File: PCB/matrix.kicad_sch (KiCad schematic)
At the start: 103 parts, among them SW10 1u, SW100 1u, SW101 1u, SW102 1u, SW103 2u, SW104 1u, SW11 1u, SW12 1u, SW13 1u, SW14 1u, SW15 1u, SW16 1u, SW17 1u, SW18 1u, SW19 1u, SW2 1u, SW20 1u, SW21 1u, SW22 1u, SW23 1u, SW24 1u, SW25 1u, SW26 1u, SW27 1u, SW28 1u, SW29 1u, SW3 1u, SW30 1u, SW31 1u, SW32 1u, SW33 1.5u, SW34 1u, SW35 1u, SW36 1u, SW37 1u, SW38 1u, SW39 1.5u, SW4 1u, SW40 1u, SW41 1u, SW42 1u, SW43 1u, SW44 1u, SW45 1u, SW46 1u, SW47 1u, SW48 1u, SW49 1u, SW5 1u, SW50 1u, SW51 1u, SW52 1u, SW53 1u, SW54 1u, SW55 1u, SW56 1u, SW57 1u, SW58 1.5u, SW59 1u, SW6 1u, SW60 1u, SW61 1u, SW62 1u, SW63 1u, SW64 1u, SW65 1u, SW66 1u, SW67 1u, SW68 1u, SW69 1u, SW7 1u, SW70 1u, SW71 1u, SW72 1.5u, SW73 1u, SW74 1u, SW75 1u, SW76 1u, SW77 1u, SW78 2.25u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

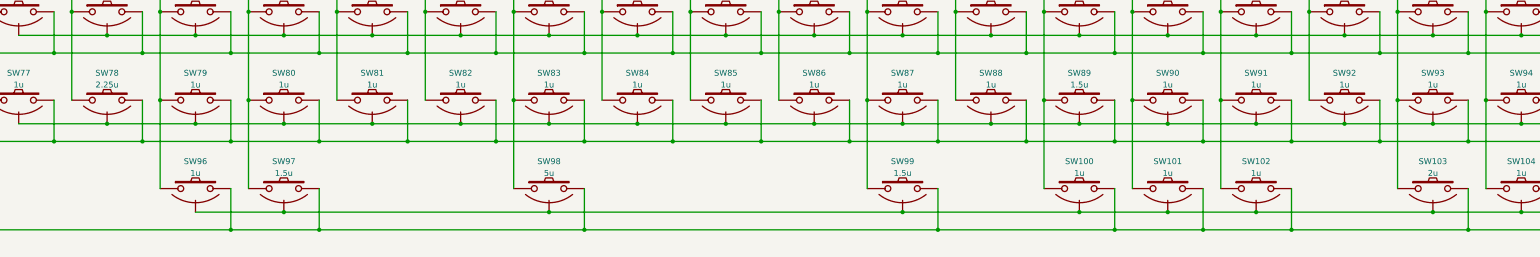
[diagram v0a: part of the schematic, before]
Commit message: Update for 3d models
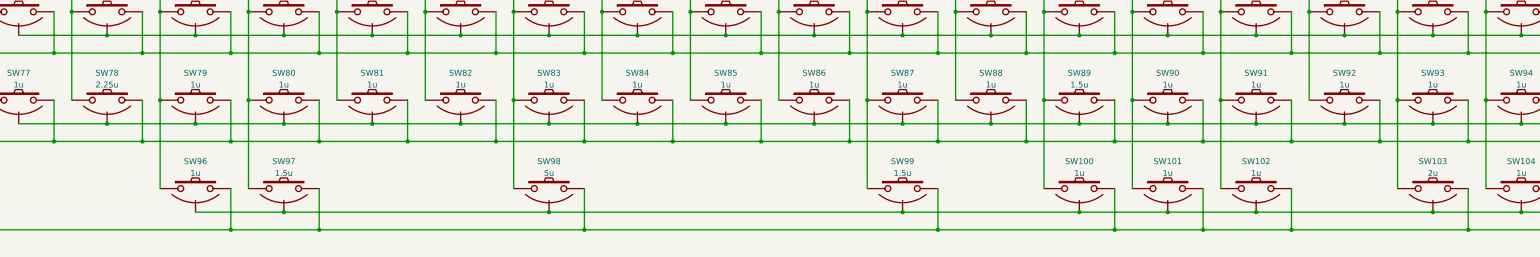
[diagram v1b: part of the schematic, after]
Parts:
- SW10, SW100, SW101, SW102, SW104, SW11, SW12, SW13, SW14, SW15, SW16, SW17, SW18, SW19, SW2, SW20, SW21, SW22, SW23, SW24, SW25, SW26, SW27, SW28, SW29, SW3, SW30, SW31, SW32, SW33, SW34, SW35, SW36, SW37, SW38, SW39, SW4, SW40, SW41, SW42, SW43, SW44, SW45, SW46, SW47, SW48, SW49, SW5, SW50, SW51, SW52, SW53, SW54, SW55, SW56, SW57, SW58, SW59, SW6, SW60, SW61, SW62, SW63, SW64, SW65, SW66, SW67, SW68, SW69, SW7, SW70, SW71, SW72, SW73, SW74, SW75, SW76, SW77, SW79, SW8, SW80, SW81, SW82, SW83, SW84, SW85, SW86, SW87, SW88, SW89, SW9, SW90, SW91, SW92, SW93, SW94, SW96, SW97, SW98, SW99: footprint cipulot_parts:ecs_pad_no_ring -> cipulot_parts:ecs_pad_1U_no_ring
- SW103, SW78, SW95: footprint cipulot_parts:ecs_pad_no_ring -> cipulot_parts:ecs_pad_2U_no_ring
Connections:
- net COL1: now also SW78.2; no longer SW78.1
- net COL16: now also SW103.2; no longer SW103.1
- net ROW4: now also SW78.1; no longer SW78.2
- net ROW5: now also SW103.1; no longer SW103.2

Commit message: Updated sheets
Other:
- company: Cipulot PCB Design  -> LU.SV Solutions
- title: CDS - Matrix -> CDS
